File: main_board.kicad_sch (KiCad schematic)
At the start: 15 parts, among them CN1 DF40C-30DS-0.4V | PWR, CN2 DF40C-30DS-0.4V | IO, J4 DF40C-100DP-0.4V51, J5 DF40C-100DP-0.4V51, SW1 RESET_L, SW2 PWRON_L, U10 SiP32508DT, U11 SiP32508DT

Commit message: Move Data USB-C Port to IO + Add USB1 SS mux and SBU orientation switch, resolve CM5 GPIO assignments
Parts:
- removed CN2: DF40C-30DS-0.4V | IO, slate113:CONN-SMD_DF40C-30DS-0.4V51, symbol slate113:DF40C-30DS-0.4V
- added C32: 2.2µF, symbol Device:C_Small
- added C33: 100nF, symbol Device:C_Small
- added U14: SiP32508DT, Package_TO_SOT_SMD:TSOT-23-6, symbol Power_Management:SiP32508DT
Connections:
- net CM5_5V: now also C32.1
- net GND: now also U14.4 (GND)
- net M2_EN: now also J4.64
- net M2_PWROFF: now also J4.68
- net USB1_DIR: now reaches J4.38
- net USB1_MUX_EN: now reaches J4.40
- new net: C33.2, U14.1 (OUT), U14.2 (OUT)
- new net: C32.2, U14.5 (IN), U14.6 (IN)
- new net USB1_PWREN: U14.3 (EN)
- new net USB1_VBUS: C33.1
- no-connect marks 89 -> 88
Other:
- note added: "IO + M.2 Connector"
- note added: "USB1 Power"
- note removed: "IO Mezzanine"
- moved on the sheet: C18, C19, C20, C21, CN1, FB2, FPC1, J4A, J4B, J5A, J5B, R17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

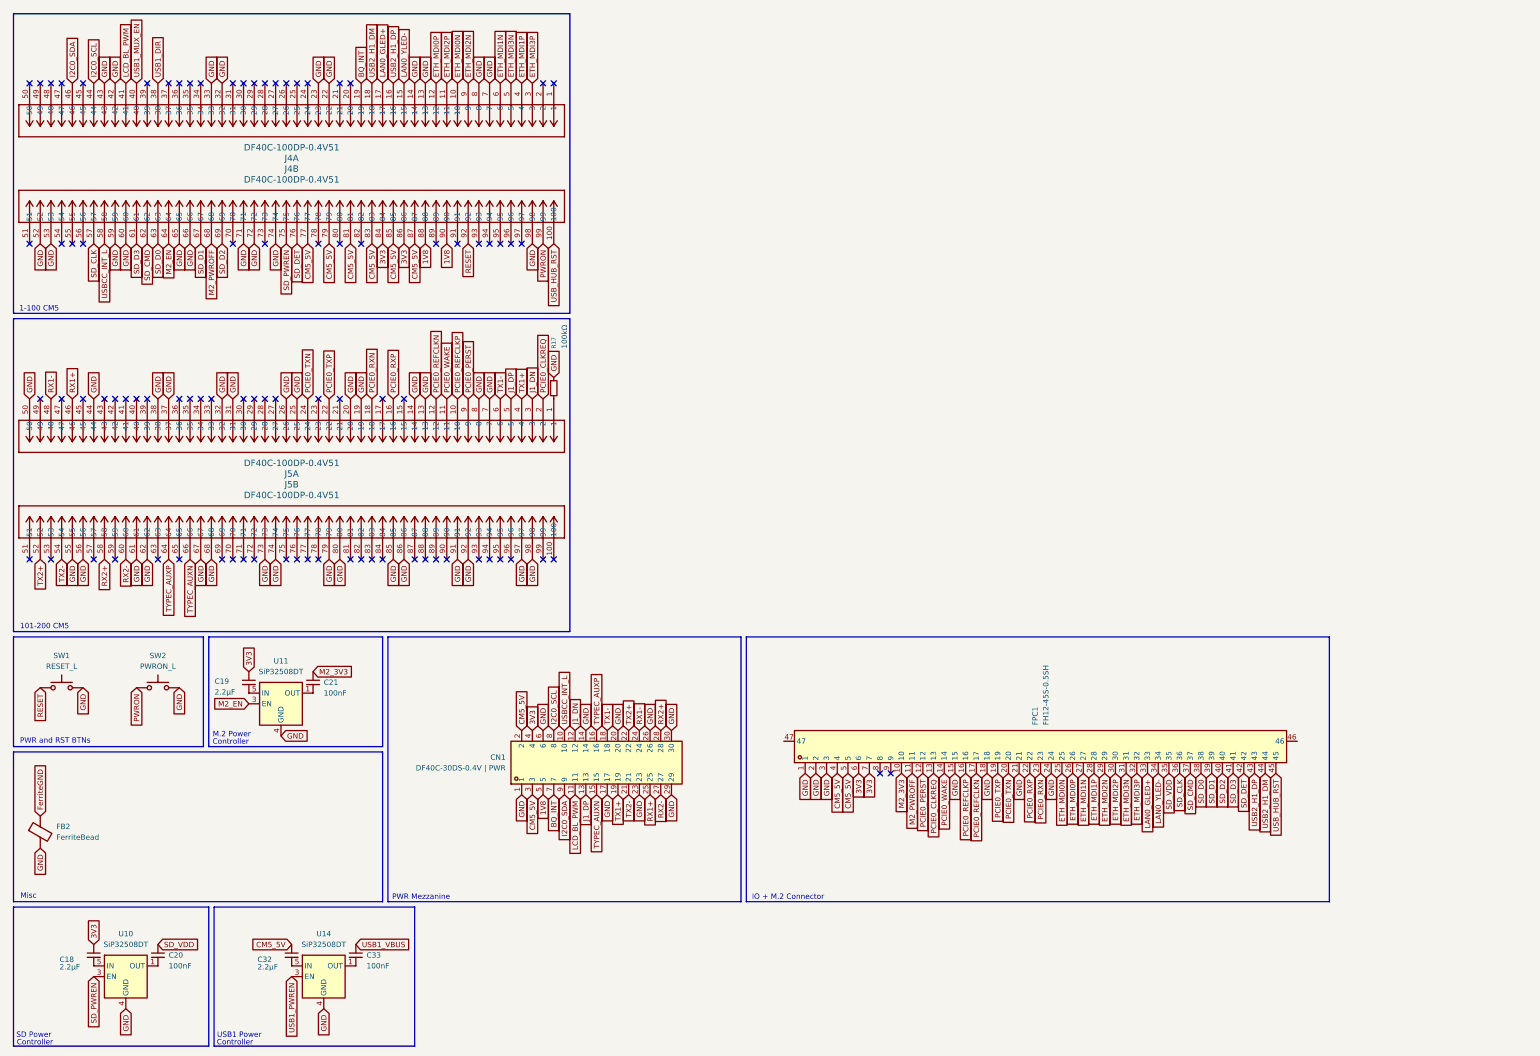
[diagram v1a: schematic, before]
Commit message: add wifi+ble combo symbol, fix connector pin counts, slim b2b connectors, drop 3-way flex cable
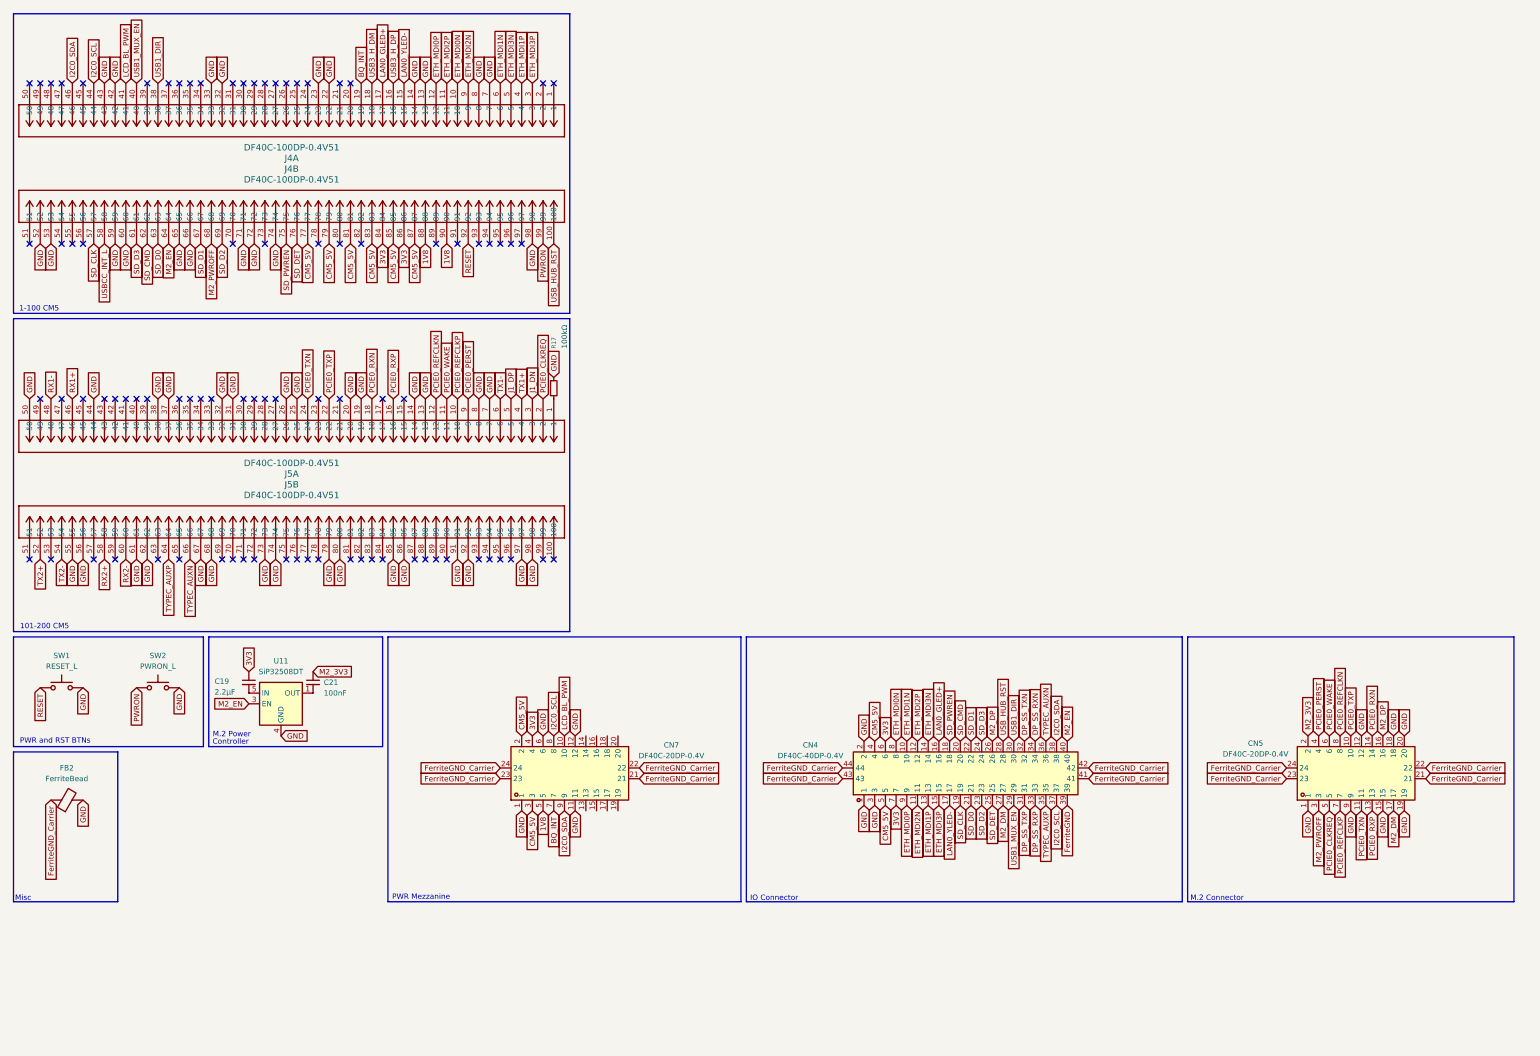
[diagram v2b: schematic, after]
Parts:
- removed C18, C32: 2.2µF, symbol Device:C_Small
- removed C20, C33: 100nF, symbol Device:C_Small
- removed CN1: DF40C-30DS-0.4V | PWR, slate113:CONN-SMD_DF40C-30DS-0.4V51, symbol slate113:DF40C-30DS-0.4V
- removed FPC1: FH12-45S-0.5SH, slate113:CONN-SMD_FH12-45S-0.5SH-55, symbol slate113:FH12-45S-0.5SH
- removed U10, U14: SiP32508DT, Package_TO_SOT_SMD:TSOT-23-6, symbol Power_Management:SiP32508DT
- added CN4: DF40C-40DP-0.4V, slate113:CONN-SMD_DF40C-40DP-0.4V, symbol slate113:DF40C-40DP-0.4V
- added CN5, CN7: DF40C-20DP-0.4V, slate113:CONN-SMD_20P-P0.40_HRS_DF40TC-20DP-0.4V, symbol slate113:DF40C-20DP-0.4V
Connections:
- net 1V8: now also CN7.5
- net 3V3: now also CN4.6, CN4.7, CN7.4
- net BQ_INT: now also CN7.7
- net CM5_5V: now also CN4.4, CN4.5, CN7.2, CN7.3
- net ETH_MDI0N: now also CN4.8
- net ETH_MDI0P: now also CN4.9
- net ETH_MDI1N: now also CN4.10
- net ETH_MDI1P: now also CN4.13
- net ETH_MDI2N: now also CN4.11
- net ETH_MDI2P: now also CN4.12
- net ETH_MDI3N: now also CN4.14
- net ETH_MDI3P: now also CN4.15
- net FerriteGND: now also CN4.39; no longer FB2.1
- net GND: now also CN4.1, CN4.2, CN4.3, CN5.1, CN5.12, CN5.15, CN5.18, CN5.19, CN5.20, CN5.9, CN7.1, CN7.11, CN7.12, CN7.6
- net I2C0_SCL: now also CN4.37, CN7.8
- net I2C0_SDA: now also CN4.38, CN7.9
- net LAN0_GLED+: now also CN4.16
- net LAN0_YLED-: now also CN4.17
- net LCD_BL_PWM: now also CN7.10
- net M2_3V3: now also CN5.2
- net M2_EN: now also CN4.40
- net M2_PWROFF: now also CN5.3
- net PCIE0_CLKREQ: now also CN5.5
- net PCIE0_PERST: now also CN5.4
- net PCIE0_REFCLKN: now also CN5.8
- net PCIE0_REFCLKP: now also CN5.7
- net PCIE0_RXN: now also CN5.14
- net PCIE0_RXP: now also CN5.13
- net PCIE0_TXN: now also CN5.11
- net PCIE0_TXP: now also CN5.10
- net PCIE0_WAKE: now also CN5.6
- net SD_CLK: now also CN4.19
- net SD_CMD: now also CN4.20
- net SD_D0: now also CN4.21
- net SD_D1: now also CN4.22
- net SD_D2: now also CN4.23
- net SD_D3: now also CN4.24
- net SD_DET: now also CN4.25
- net SD_PWREN: now also CN4.18
- net TYPEC_AUXN: now also CN4.36
- net TYPEC_AUXP: now also CN4.35
- net USB1_DIR: now also CN4.30
- net USB1_MUX_EN: now also CN4.29
- net USB_HUB_RST: now also CN4.28
- net USB2_H1_DM renamed USB3_H_DM
- net USB2_H1_DP renamed USB3_H_DP
- new net DP_SS_RXN: CN4.34
- new net DP_SS_RXP: CN4.33
- new net DP_SS_TXN: CN4.32
- new net DP_SS_TXP: CN4.31
- new net FerriteGND_Carrier: CN4.41, CN4.42, CN4.43, CN4.44, CN5.21, CN5.22, CN5.23, CN5.24, CN7.21, CN7.22, CN7.23, CN7.24, FB2.1
- new net M2_DM: CN4.27, CN5.17
- new net M2_DP: CN4.26, CN5.16
- no-connect marks 88 -> 86
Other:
- note added: "IO Connector"
- note added: "M.2 Connector"
- note removed: "IO + M.2 Connector"
- note removed: "SD Power"
- note removed: "USB1 Power"
- moved on the sheet: FB2

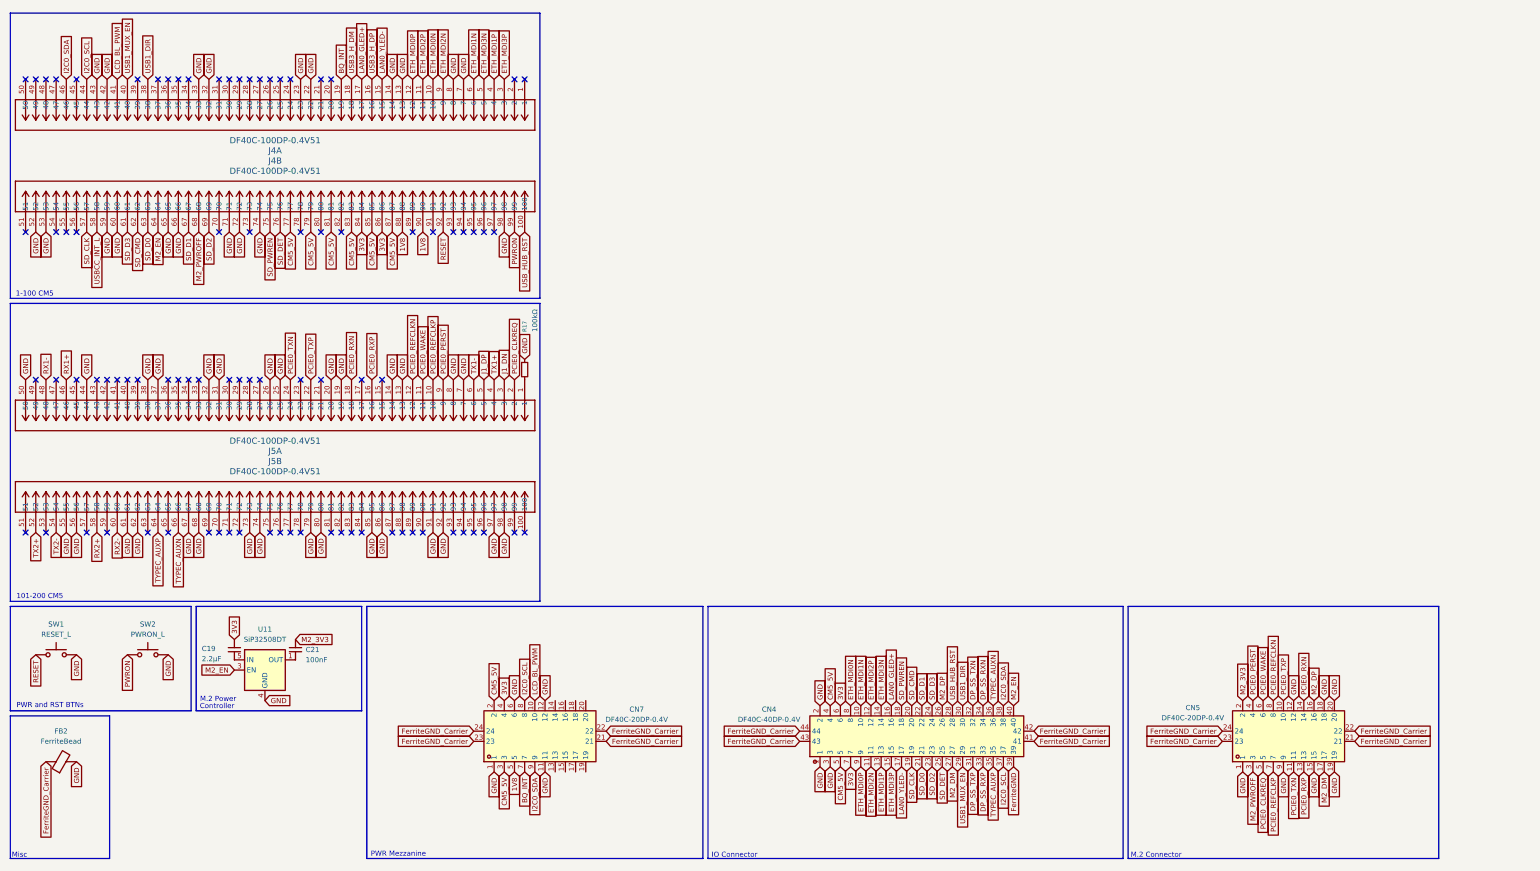
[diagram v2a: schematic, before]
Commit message: finish wiring up usb hub + fix stale nets + address DRC errors
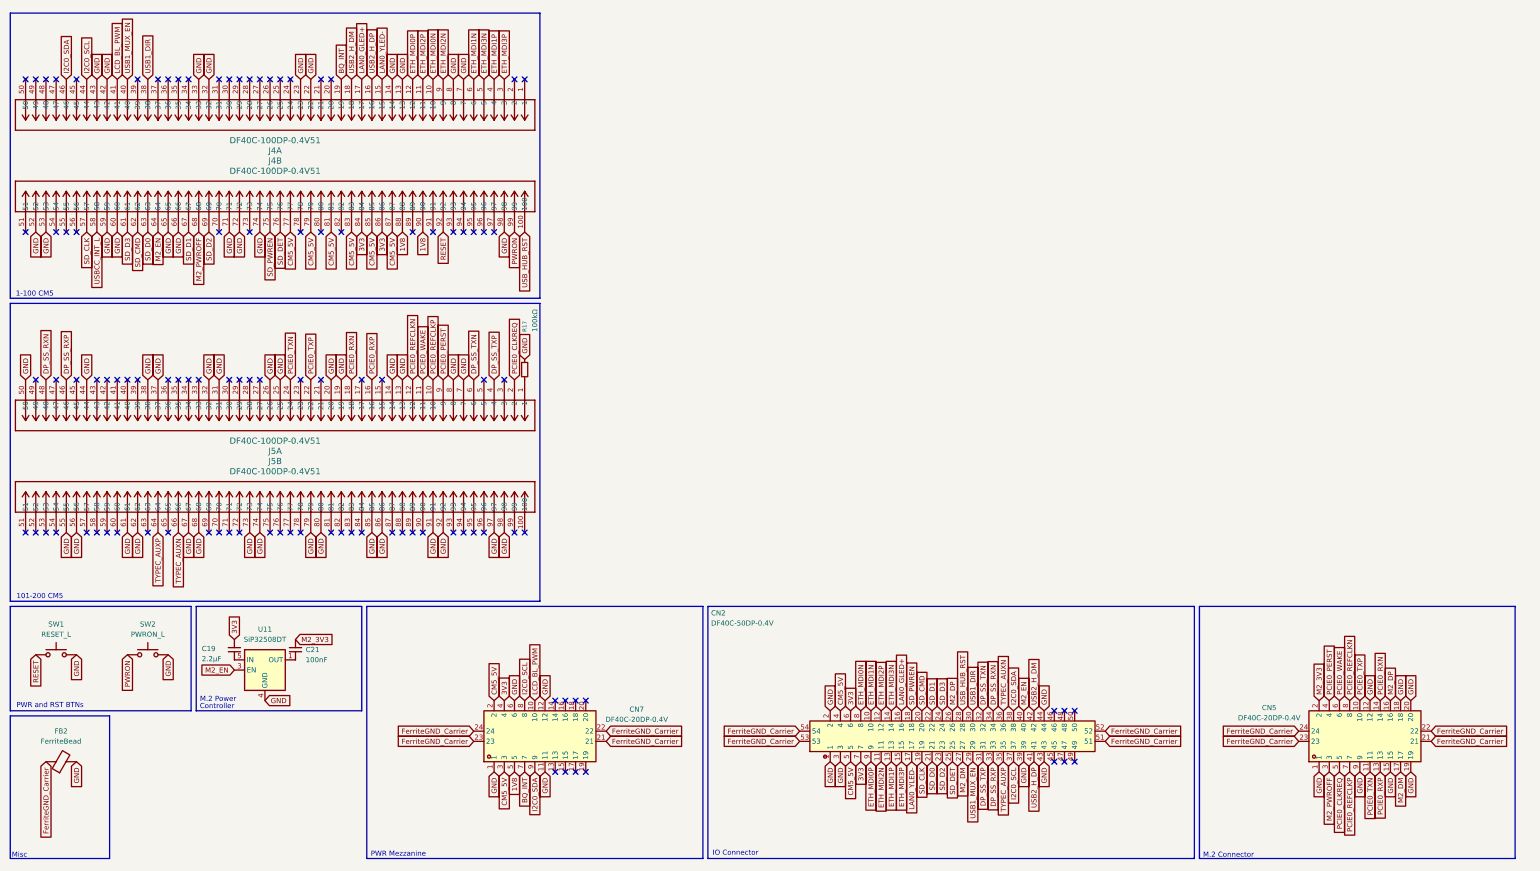
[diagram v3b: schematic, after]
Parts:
- removed CN4: DF40C-40DP-0.4V, slate113:CONN-SMD_DF40C-40DP-0.4V, symbol slate113:DF40C-40DP-0.4V
- added CN2: DF40C-50DP-0.4V, slate113:CONN-SMD_DF40C-50DP-0.4V, symbol slate113:DF40C-50DP-0.4V
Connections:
- net RX1+ is gone; now on net DP_SS_RXP: J5.46
- net RX1- is gone; now on net DP_SS_RXN: J5.48
- net TX1+ is gone; now on net DP_SS_TXP: J5.4
- net TX1- is gone; now on net DP_SS_TXN: J5.6
- net 3V3: now also CN2.6, CN2.7
- net CM5_5V: now also CN2.4, CN2.5
- net DP_SS_RXN: now also CN2.34
- net DP_SS_RXP: now also CN2.33
- net DP_SS_TXN: now also CN2.32
- net DP_SS_TXP: now also CN2.31
- net ETH_MDI0N: now also CN2.8
- net ETH_MDI0P: now also CN2.9
- net ETH_MDI1N: now also CN2.10
- net ETH_MDI1P: now also CN2.13
- net ETH_MDI2N: now also CN2.11
- net ETH_MDI2P: now also CN2.12
- net ETH_MDI3N: now also CN2.14
- net ETH_MDI3P: now also CN2.15
- net FerriteGND_Carrier: now also CN2.51, CN2.52, CN2.53, CN2.54
- net GND: now also CN2.1, CN2.2, CN2.3, CN2.39, CN2.43, CN2.44
- net I2C0_SCL: now also CN2.37
- net I2C0_SDA: now also CN2.38
- net LAN0_GLED+: now also CN2.16
- net LAN0_YLED-: now also CN2.17
- net M2_DM: now also CN2.27
- net M2_DP: now also CN2.26
- net M2_EN: now also CN2.40
- net SD_CLK: now also CN2.19
- net SD_CMD: now also CN2.20
- net SD_D0: now also CN2.21
- net SD_D1: now also CN2.22
- net SD_D2: now also CN2.23
- net SD_D3: now also CN2.24
- net SD_DET: now also CN2.25
- net SD_PWREN: now also CN2.18
- net TYPEC_AUXN: now also CN2.36
- net TYPEC_AUXP: now also CN2.35
- net USB1_DIR: now also CN2.30
- net USB1_MUX_EN: now also CN2.29
- net USB_HUB_RST: now also CN2.28
- net J1_DN: no longer names the net of J5.3
- net J1_DP: no longer names the net of J5.5
- net RX2+: no longer names the net of J5.58
- net RX2-: no longer names the net of J5.60
- net TX2+: no longer names the net of J5.52
- net TX2-: no longer names the net of J5.54
- net USB3_H_DM renamed USB2_H_DM
- net USB2_H_DM: now also CN2.42
- net USB3_H_DP renamed USB2_H_DP
- net USB2_H_DP: now also CN2.41
- no-connect marks 86 -> 106
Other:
- moved on the sheet: CN5

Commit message: forgot to save
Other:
- note added: "PWR Declarations"
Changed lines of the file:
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@@
 	)
 	(rectangle
+		(start 40.005 189.23)
+		(end 101.6 224.79)
+		(stroke
+			(width 0)
+			(type default)
+		)
+		(fill
+			(type none)
+		)
+	)
+	(rectangle
 		(start 13.97 189.23)
 		(end 38.735 224.79)
@@
 		)
 	)
+	(text "PWR Declarations"
+		(exclude_from_sim no)
+		(at 48.768 224.028 0)
+		(effects
+			(font
+				(size 1.27 1.27)
+			)
+		)
+	)
 	(text "M.2 Connector\n"
 		(exclude_from_sim no)
@@
 		)
 	)
+	(junction
+		(at 69.85 175.26)
+		(diameter 0)
+		(color 0 0 0 0)
+	)
 	(no_connect
 		(at 60.96 105.41)
@@
 		)
 	)
+	(global_label "M2_EN"
+		(shape input)
+		(at 43.18 199.39 90)
+		(fields_autoplaced yes)
+		(effects
+			(font
+				(size 1.27 1.27)
+			)
+			(justify left)
+		)
+		(property "Intersheetrefs" "${INTERSHEET_REFS}"
+			(at 43.18 190.2968 90)
+			(hide yes)
+			(show_name no)
+			(do_not_autoplace no)
+			(effects
+				(font
+					(size 1.27 1.27)
+				)
+				(justify left)
+			)
+		)
+	)
 	(global_label "SD_D0"
 		(shape input)
@@
 	)
 	(symbol
+		(lib_id "power:PWR_FLAG")
+		(at 43.18 199.39 180)
+		(unit 1)
+		(body_style 1)
+		(exclude_from_sim no)
+		(in_bom yes)
+		(on_board yes)
+		(in_pos_files yes)
+		(dnp no)
+		(fields_autoplaced yes)
+		(property "Reference" "#FLG014"
+			(at 43.18 201.295 0)
+			(hide yes)
+			(show_name no)
+			(do_not_autoplace no)
+			(effects
+				(font
+					(size 1.27 1.27)
+				)
+			)
+		)
+		(property "Value" "PWR_FLAG"
+			(at 43.18 204.47 0)
+			(hide yes)
+			(show_name no)
+			(do_not_autoplace no)
+			(effects
+				(font
+					(size 1.27 1.27)
+				)
+			)
+		)
+		(property "Footprint" ""
+			(at 43.18 199.39 0)
+			(hide yes)
+			(show_name no)
+			(do_not_autoplace no)
+			(effects
+				(font
+					(size 1.27 1.27)
+				)
+			)
+		)
+		(property "Datasheet" ""
+			(at 43.18 199.39 0)
+			(hide yes)
+			(show_name no)
+			(do_not_autoplace no)
+			(effects
+				(font
+					(size 1.27 1.27)
+				)
+			)
+		)
+		(property "Description" "Special symbol for telling ERC where power comes from"
+			(at 43.18 199.39 0)
+			(hide yes)
+			(show_name no)
+			(do_not_autoplace no)
+			(effects
+				(font
+					(size 1.27 1.27)
+				)
+			)
+		)
+		(pin "1"
+		)
+		(instances
+			(project "slate113"
+				(path "/9f5acde0-c32a-42eb-a9f2-f6cec9b16f5a"
+					(reference "#FLG014")
+					(unit 1)
+				)
+			)
+		)
+	)
+	(symbol
 		(lib_id "slate113:DF40C-100DP-0.4V51")
 		(at 17.78 143.51 90)
@@
 					(unit 1)
 				)
+			)
+		)
+	)
+	(symbol
+		(lib_id "power:PWR_FLAG")
+		(at 69.85 175.26 90)
+		(unit 1)
+		(body_style 1)
+		(exclude_from_sim no)
+		(in_bom yes)
+		(on_board yes)
+		(in_pos_files yes)
+		(dnp no)
+		(fields_autoplaced yes)
+		(property "Reference" "#FLG015"
+			(at 67.945 175.26 0)
+			(hide yes)
+			(show_name no)
+			(do_not_autoplace no)
+			(effects
+				(font
+					(size 1.27 1.27)
+				)
+			)
+		)
+		(property "Value" "PWR_FLAG"
+			(at 64.77 175.26 0)
+			(hide yes)
+			(show_name no)
+			(do_not_autoplace no)
+			(effects
+				(font
+					(size 1.27 1.27)
+				)
+			)
+		)
+		(property "Footprint" ""
+			(at 69.85 175.26 0)
+			(hide yes)
+			(show_name no)
+			(do_not_autoplace no)
+			(effects
+				(font
+					(size 1.27 1.27)
+				)
+			)
+		)
+		(property "Datasheet" ""
+			(at 69.85 175.26 0)
+			(hide yes)
+			(show_name no)
+			(do_not_autoplace no)
+			(effects
+				(font
+					(size 1.27 1.27)
+				)
+			)
+		)
+		(property "Description" "Special symbol for telling ERC where power comes from"
+			(at 69.85 175.26 0)
+			(hide yes)
+			(show_name no)
+			(do_not_autoplace no)
+			(effects
+				(font
+					(size 1.27 1.27)
+				)
+			)
+		)
+		(pin "1"
+		)
+		(instances
+			(project "slate113"
+				(path "/9f5acde0-c32a-42eb-a9f2-f6cec9b16f5a"
+					(reference "#FLG015")
+					(unit 1)
+				)

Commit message: finished radio board with load switches and flash, fixed b2b connector, started antenna module and rf sense switching circuit
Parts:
- added CN20: DF40C-20DP-0.4V, slate113:CONN-SMD_20P-P0.40_HRS_DF40TC-20DP-0.4V, symbol slate113:DF40C-20DP-0.4V
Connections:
- net 3V3: now also CN20.7
- net GND: now also CN20.1, CN20.10, CN20.11, CN20.12, CN20.3, CN20.5
- new net 5V: CN20.9
- new net CM5_UART_RX: CN20.4
- new net CM5_UART_TX: CN20.2
- new net FerriteGND_RADIO: CN20.21, CN20.22, CN20.23, CN20.24
- new net RADIO_EN: CN20.8
- new net RP_RST: CN20.6
- no-connect marks 106 -> 114
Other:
- note added: "Main > Radio"
- moved on the sheet: CN5
